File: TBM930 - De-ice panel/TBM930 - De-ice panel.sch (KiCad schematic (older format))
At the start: 64 parts, among them J1 SW_AIRFRAME_DE_ICE, J10 AVR-ISP-6, J2 SW_ICE_LIGHT, J3 SW_PROP_DE_ICE, J4 SW_WIND_SHIELD, J5 SW_PITOT_L_HTR, J6 SW_PITOT_R_HTR, J7 SW_INERT_SEP, J8 Barrel_Jack, J9 USB_B_Micro, SW1 SW_Push, SW2 SW_Push, U1 TLC5917IN, U2 TLC5917IN, U3 ATmega32U4-MU, Y1 Crystal_GND24

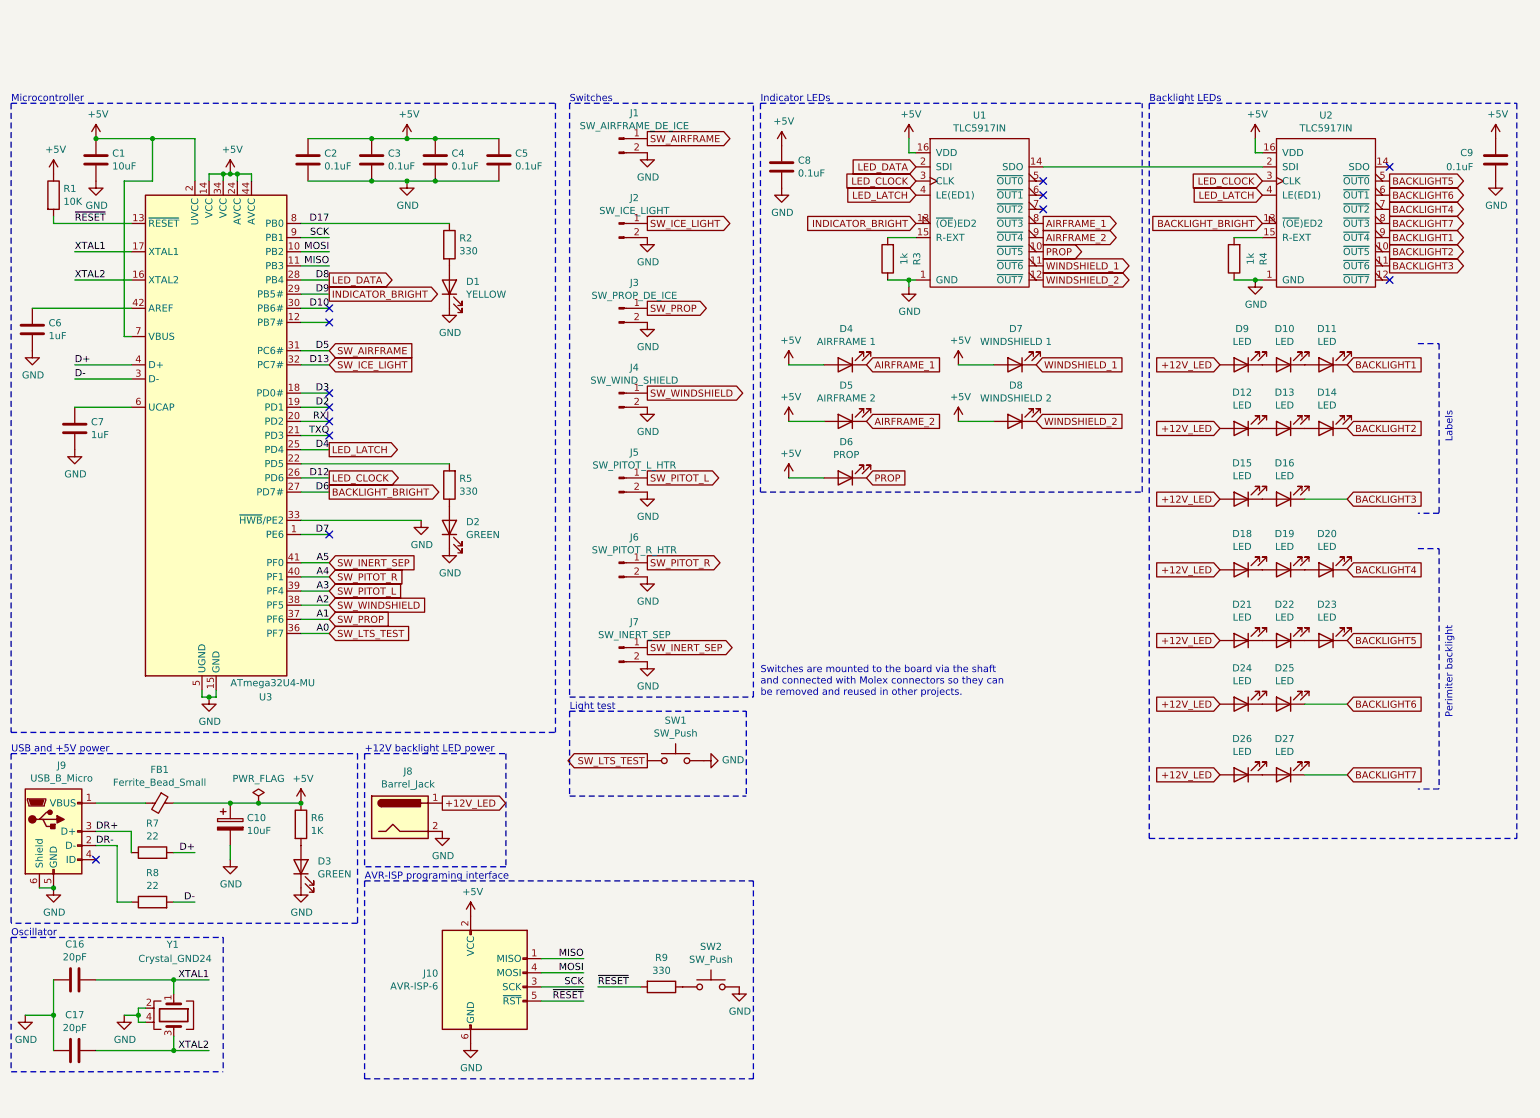
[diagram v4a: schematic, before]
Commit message: Additional reset components
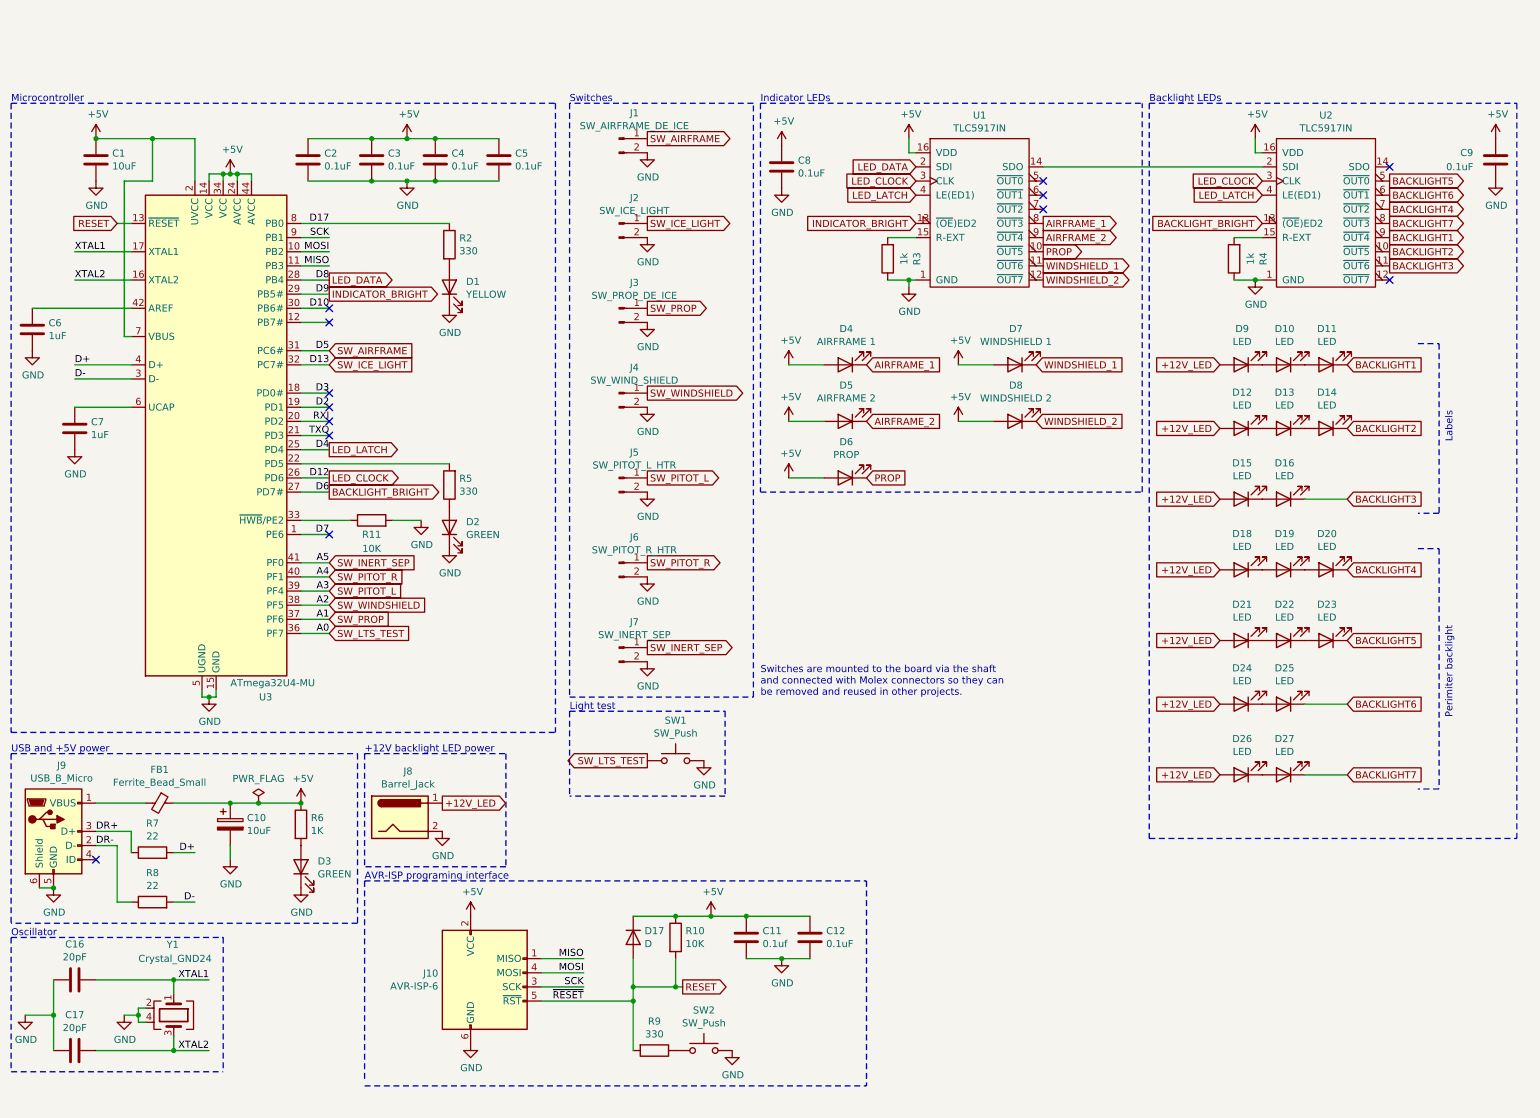
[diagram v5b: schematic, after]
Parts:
- removed R1: 10K, Resistor_SMD:R_0603_1608Metric, symbol Device:R
- added C11: 0.1uf, Capacitor_SMD:C_0603_1608Metric, symbol Device:C
- added C12: 0.1uF, Capacitor_SMD:C_0603_1608Metric, symbol Device:C
- added D17: D, Diode_SMD:D_SOD-323F, symbol Device:D
- added R10, R11: 10K, Resistor_SMD:R_0603_1608Metric, symbol Device:R
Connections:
- net +5V: now also C11.1, C12.1, D17.1 (K), R10.1
- net GND: now also C11.2, C12.2, R11.2; no longer U3.33 (~HWB~/PE2)
- net ~RESET renamed RESET
- net RESET: now also D17.2 (A), R10.2
- new net: R11.1, U3.33 (~HWB~/PE2)
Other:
- moved on the sheet: R9, SW2
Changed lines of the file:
@@
 Text Notes 5800 4800 0    50   ~ 0
 Switches are mounted to the board via the shaft\nand connected with Molex connectors so they can\nbe removed and reused in other projects.\n
-$Comp
-L power:GND #PWR034
-U 1 1 611957DA
-P 5400 5250
-F 0 "#PWR034" H 5400 5000 50  0001 C CNN
-F 1 "GND" V 5405 5122 50  0000 R CNN
-F 2 "" H 5400 5250 50  0001 C CNN
-F 3 "" H 5400 5250 50  0001 C CNN
-	1    5400 5250
-	0    -1   -1   0
-$EndComp
 Text GLabel 5000 5250 0    50   Output ~ 0
 SW_LTS_TEST
@@
 Wire Notes Line
 	8550 600  11150 600
-$Comp
-L Switch:SW_Push SW1
-U 1 1 611D77B6
-P 5200 5250
-F 0 "SW1" H 5200 5535 50  0000 C CNN
-F 1 "SW_Push" H 5200 5444 50  0000 C CNN
-F 2 "Button_Switch_THT:SW_PUSH_6mm_H9.5mm" H 5200 5450 50  0001 C CNN
-F 3 "~" H 5200 5450 50  0001 C CNN
-F 4 "0603" H 5200 5250 50  0001 C CNN "JLC"
-	1    5200 5250
-	1    0    0    -1
-$EndComp
 Text GLabel 9050 4850 0    50   Input ~ 0
 +12V_LED
@@
 $EndComp
 Wire Wire Line
-	4250 6650 4550 6650
-Wire Wire Line
 	4250 6750 4550 6750
 Wire Wire Line
@@
 Text Label 4550 6850 2    50   ~ 0
 SCK
-Wire Wire Line
-	4250 6950 4550 6950
 Text Label 4550 6950 2    50   ~ 0
 ~RESET
-Text Label 950  1450 0    50   ~ 0
-~RESET
 Wire Notes Line
 	3000 6100 3000 7500
-Wire Notes Line
-	5750 7500 5750 6100
 Text Notes 3000 6100 0    50   ~ 0
 AVR-ISP programing interface
@@
 Wire Wire Line
 	2050 5850 2050 5950
-$Comp
-L Device:R R1
-U 1 1 61244DA8
-P 800 1250
-F 0 "R1" H 870 1296 50  0000 L CNN
-F 1 "10K" H 870 1205 50  0000 L CNN
-F 2 "Resistor_SMD:R_0603_1608Metric" V 730 1250 50  0001 C CNN
-F 3 "~" H 800 1250 50  0001 C CNN
-F 4 "0603" H 800 1250 50  0001 C CNN "JLC"
-F 5 "C25804" H 800 1250 50  0001 C CNN "LCSC"
-	1    800  1250
-	1    0    0    -1
-$EndComp
-Wire Wire Line
-	800  1450 1350 1450
-Wire Wire Line
-	800  1400 800  1450
-$Comp
-L power:+5V #PWR06
-U 1 1 6127B47C
-P 800 1100
-F 0 "#PWR06" H 800 950 50  0001 C CNN
-F 1 "+5V" H 815 1273 50  0000 C CNN
-F 2 "" H 800 1100 50  0001 C CNN
-F 3 "" H 800 1100 50  0001 C CNN
-	1    800  1100
-	1    0    0    -1
-$EndComp
-$Comp
-L Switch:SW_Push SW2
-U 1 1 611E6C32
-P 5450 6850
-F 0 "SW2" H 5450 7135 50  0000 C CNN
-F 1 "SW_Push" H 5450 7044 50  0000 C CNN
-F 2 "Button_Switch_THT:SW_PUSH_6mm_H4.3mm" H 5450 7050 50  0001 C CNN
-F 3 "~" H 5450 7050 50  0001 C CNN
-F 4 "0603" H 5450 6850 50  0001 C CNN "JLC"
-	1    5450 6850
-	1    0    0    -1
-$EndComp
-Text Label 4650 6850 0    50   ~ 0
-~RESET
-Wire Wire Line
-	4950 6850 4650 6850
-$Comp
-L power:GND #PWR037
-U 1 1 611F4AE3
-P 5650 6850
-F 0 "#PWR037" H 5650 6600 50  0001 C CNN
-F 1 "GND" H 5655 6677 50  0000 C CNN
-F 2 "" H 5650 6850 50  0001 C CNN
-F 3 "" H 5650 6850 50  0001 C CNN
-	1    5650 6850
-	1    0    0    -1
-$EndComp
 Wire Wire Line
 	1100 5550 1450 5550
@@
 DR-
 Wire Wire Line
-	2550 3550 3400 3550
+	2550 3550 2900 3550
 $Comp
 L Device:C C2
@@
 L Device:R R9
 U 1 1 612543FE
-P 5100 6850
-F 0 "R9" V 4893 6850 50  0000 C CNN
-F 1 "330" V 4984 6850 50  0000 C CNN
-F 2 "Resistor_SMD:R_0603_1608Metric" V 5030 6850 50  0001 C CNN
-F 3 "~" H 5100 6850 50  0001 C CNN
-F 4 "0603" H 5100 6850 50  0001 C CNN "JLC"
-F 5 "C23138" H 5100 6850 50  0001 C CNN "LCSC"
-	1    5100 6850
+P 5050 7300
+F 0 "R9" V 4843 7300 50  0000 C CNN
+F 1 "330" V 4934 7300 50  0000 C CNN
+F 2 "Resistor_SMD:R_0603_1608Metric" V 4980 7300 50  0001 C CNN
+F 3 "~" H 5050 7300 50  0001 C CNN
+F 4 "0603" H 5050 7300 50  0001 C CNN "JLC"
+F 5 "C23138" H 5050 7300 50  0001 C CNN "LCSC"
+	1    5050 7300
 	0    1    1    0
 $EndComp
@@
 Wire Notes Line
 	3000 5200 3000 6000
-Wire Notes Line
-	3000 6100 5750 6100
-Wire Notes Line
-	3000 7500 5750 7500
 $Comp
 L Global_MobiFlight_panel_parts:ATmega32U4-MU U3
@@
 Wire Wire Line
 	2000 1100 2050 1100
-Wire Notes Line
-	4450 5500 5700 5500
-Wire Notes Line
-	5700 4900 5700 5500
-Wire Notes Line
-	4450 4900 5700 4900
 NoConn ~ 10250 1850
 $Comp
@@
 Wire Notes Line
 	8500 3350 8500 600
+$Comp
+L Device:D D17
+U 1 1 61212341
+P 4900 6500
+F 0 "D17" V 4854 6580 50  0000 L CNN
+F 1 "D" V 4945 6580 50  0000 L CNN
+F 2 "Diode_SMD:D_SOD-323F" H 4900 6500 50  0001 C CNN
+F 3 "~" H 4900 6500 50  0001 C CNN
+F 4 "SOD-323F" H 4900 6500 50  0001 C CNN "JLC"
+F 5 "C2128" H 4900 6500 50  0001 C CNN "LCSC"
+	1    4900 6500
+	0    1    1    0
+$EndComp
+$Comp
+L Device:R R10
+U 1 1 6121292A
+P 5200 6500
+F 0 "R10" H 5270 6546 50  0000 L CNN
+F 1 "10K" H 5270 6455 50  0000 L CNN
+F 2 "Resistor_SMD:R_0603_1608Metric" V 5130 6500 50  0001 C CNN
+F 3 "~" H 5200 6500 50  0001 C CNN
+F 4 "0603" H 5200 6500 50  0001 C CNN "JLC"
+F 5 "C25804" H 5200 6500 50  0001 C CNN "LCSC"
+	1    5200 6500
+	1    0    0    -1
+$EndComp
+$Comp
+L Device:C C11
+U 1 1 61213D7C
+P 5700 6500
+F 0 "C11" H 5815 6546 50  0000 L CNN
+F 1 "0.1uf" H 5815 6455 50  0000 L CNN
+F 2 "Capacitor_SMD:C_0603_1608Metric" H 5738 6350 50  0001 C CNN
+F 3 "~" H 5700 6500 50  0001 C CNN
+F 4 "0603" H 5700 6500 50  0001 C CNN "JLC"
+F 5 "C14663" H 5700 6500 50  0001 C CNN "LCSC"
+	1    5700 6500
+	1    0    0    -1
+$EndComp
+$Comp
+L Device:C C12
+U 1 1 61213EAB
+P 6150 6500
+F 0 "C12" H 6265 6546 50  0000 L CNN
+F 1 "0.1uF" H 6265 6455 50  0000 L CNN
+F 2 "Capacitor_SMD:C_0603_1608Metric" H 6188 6350 50  0001 C CNN
+F 3 "~" H 6150 6500 50  0001 C CNN
+F 4 "0603" H 6150 6500 50  0001 C CNN "JLC"
+F 5 "C14663" H 6150 6500 50  0001 C CNN "LCSC"
+	1    6150 6500
+	1    0    0    -1
+$EndComp
+Wire Wire Line
+	5700 6350 6150 6350
+Wire Wire Line
+	5700 6650 5950 6650
+Wire Wire Line
+	4900 6350 5200 6350
+Wire Wire Line
+	5200 6350 5450 6350
+Connection ~ 5200 6350
+Connection ~ 5700 6350
+$Comp
+L power:+5V #PWR0107
+U 1 1 6124AEAC
+P 5450 6350
+F 0 "#PWR0107" H 5450 6200 50  0001 C CNN
+F 1 "+5V" H 5465 6523 50  0000 C CNN
+F 2 "" H 5450 6350 50  0001 C CNN
+F 3 "" H 5450 6350 50  0001 C CNN
+	1    5450 6350
+	1    0    0    -1
+$EndComp
+Connection ~ 5450 6350
+Wire Wire Line
+	5450 6350 5700 6350
+$Comp
+L power:GND #PWR0108
+U 1 1 6124B8BB
+P 5950 6650
+F 0 "#PWR0108" H 5950 6400 50  0001 C CNN
+F 1 "GND" H 5955 6477 50  0000 C CNN
+F 2 "" H 5950 6650 50  0001 C CNN
+F 3 "" H 5950 6650 50  0001 C CNN
+	1    5950 6650
+	1    0    0    -1
+$EndComp
+Connection ~ 5950 6650
+Wire Wire Line
+	5950 6650 6150 6650
+Wire Wire Line
+	4550 6650 4250 6650
+$Comp
+L Device:R R11
+U 1 1 612BF27B
+P 3050 3550
+F 0 "R11" V 2950 3550 50  0000 C CNN
+F 1 "10K" V 2850 3550 50  0000 C CNN
+F 2 "Resistor_SMD:R_0603_1608Metric" V 2980 3550 50  0001 C CNN
+F 3 "~" H 3050 3550 50  0001 C CNN
+F 4 "0603" H 3050 3550 50  0001 C CNN "JLC"
+F 5 "C25804" H 3050 3550 50  0001 C CNN "LCSC"
+	1    3050 3550
+	0    -1   -1   0
+$EndComp
+Wire Wire Line
+	3200 3550 3400 3550
+Wire Wire Line
+	4900 6650 4900 6850
+Wire Wire Line
+	4900 6850 5200 6850
+Wire Wire Line
+	5200 6850 5200 6650
+Wire Wire Line
+	4900 6950 4900 6850
+Wire Wire Line
+	4250 6950 4900 6950
+Connection ~ 4900 6850
+Wire Wire Line
+	4900 7300 4900 6950
+Connection ~ 4900 6950
+Wire Wire Line
+	5250 6850 5200 6850
+Connection ~ 5200 6850
+Text GLabel 1250 1450 0    50   Input ~ 0
+RESET
+Wire Wire Line
+	1250 1450 1350 1450
+$Comp
+L Switch:SW_Push SW1
+U 1 1 611D77B6
+P 5200 5250
+F 0 "SW1" H 5200 5535 50  0000 C CNN
+F 1 "SW_Push" H 5200 5444 50  0000 C CNN
+F 2 "Button_Switch_THT:SW_PUSH_6mm_H9.5mm" H 5200 5450 50  0001 C CNN
+F 3 "~" H 5200 5450 50  0001 C CNN
+F 4 "0603" H 5200 5250 50  0001 C CNN "JLC"
+	1    5200 5250
+	1    0    0    -1
+$EndComp
+$Comp
+L power:GND #PWR037
+U 1 1 611F4AE3
+P 5600 7300
+F 0 "#PWR037" H 5600 7050 50  0001 C CNN
+F 1 "GND" H 5605 7127 50  0000 C CNN
+F 2 "" H 5600 7300 50  0001 C CNN
+F 3 "" H 5600 7300 50  0001 C CNN
+	1    5600 7300
+	1    0    0    -1
+$EndComp
+$Comp
+L Switch:SW_Push SW2
+U 1 1 611E6C32
+P 5400 7300
+F 0 "SW2" H 5400 7585 50  0000 C CNN
+F 1 "SW_Push" H 5400 7494 50  0000 C CNN
+F 2 "Button_Switch_THT:SW_PUSH_6mm_H4.3mm" H 5400 7500 50  0001 C CNN
+F 3 "~" H 5400 7500 50  0001 C CNN
+F 4 "0603" H 5400 7300 50  0001 C CNN "JLC"
+	1    5400 7300
+	1    0    0    -1
+$EndComp
+Text GLabel 5250 6850 2    50   Output ~ 0
+RESET
+Wire Notes Line
+	6550 6100 6550 7550
+Wire Notes Line
+	3000 7550 6550 7550
+Wire Notes Line
+	3000 6100 6550 6100
+$Comp
+L power:GND #PWR?
+U 1 1 6140136F
+P 5400 5250
+F 0 "#PWR?" H 5400 5000 50  0001 C CNN
+F 1 "GND" H 5405 5077 50  0000 C CNN
+F 2 "" H 5400 5250 50  0001 C CNN
+F 3 "" H 5400 5250 50  0001 C CNN
+	1    5400 5250
+	1    0    0    -1
+$EndComp
+Wire Notes Line
+	4450 4900 5550 4900
+Wire Notes Line
+	5550 4900 5550 5500
+Wire Notes Line
+	5550 5500 4450 5500
 $EndSCHEMATC

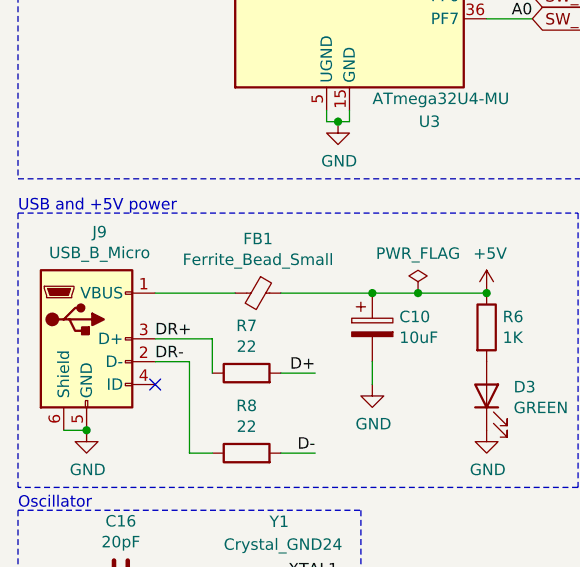
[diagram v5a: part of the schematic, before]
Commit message: Fix 12V routing
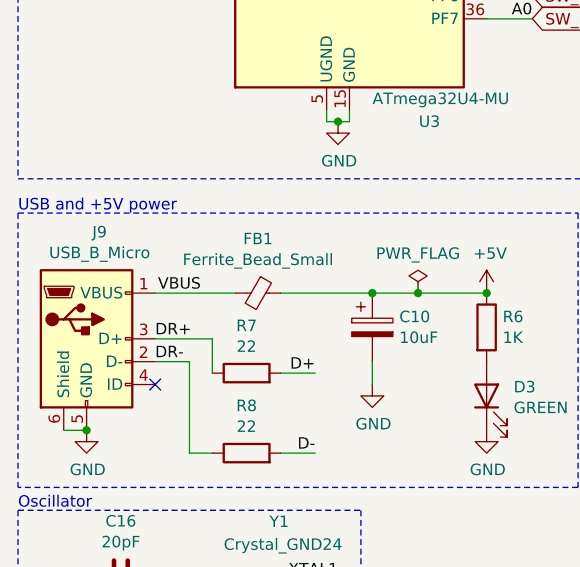
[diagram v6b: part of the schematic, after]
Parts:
- J9: footprint Connector_USB:USB_Micro-B_Molex-105017-0001 -> Global MobiFlight panel parts:USB_A_Molex_105057_Vertical
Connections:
- net VBUS: now reaches FB1.2, J9.1 (VBUS)
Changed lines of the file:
@@
 F 0 "J9" H 857 6217 50  0000 C CNN
 F 1 "USB_B_Micro" H 857 6126 50  0000 C CNN
-F 2 "Connector_USB:USB_Micro-B_Molex-105017-0001" H 950 5700 50  0001 C CNN
+F 2 "Global MobiFlight panel parts:USB_A_Molex_105057_Vertical" H 950 5700 50  0001 C CNN
 F 3 "~" H 950 5700 50  0001 C CNN
 	1    800  5750
@@
 	3000 6100 6550 6100
 $Comp
-L power:GND #PWR?
+L power:GND #PWR0109
 U 1 1 6140136F
 P 5400 5250
-F 0 "#PWR?" H 5400 5000 50  0001 C CNN
+F 0 "#PWR0109" H 5400 5000 50  0001 C CNN
 F 1 "GND" H 5405 5077 50  0000 C CNN
 F 2 "" H 5400 5250 50  0001 C CNN
@@
 Wire Notes Line
 	5550 5500 4450 5500
+Text Label 1300 5550 2    50   ~ 0
+VBUS
 $EndSCHEMATC
